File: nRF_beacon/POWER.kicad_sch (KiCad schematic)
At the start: 6 parts, among them U3 NPM1300-QEAA-R7

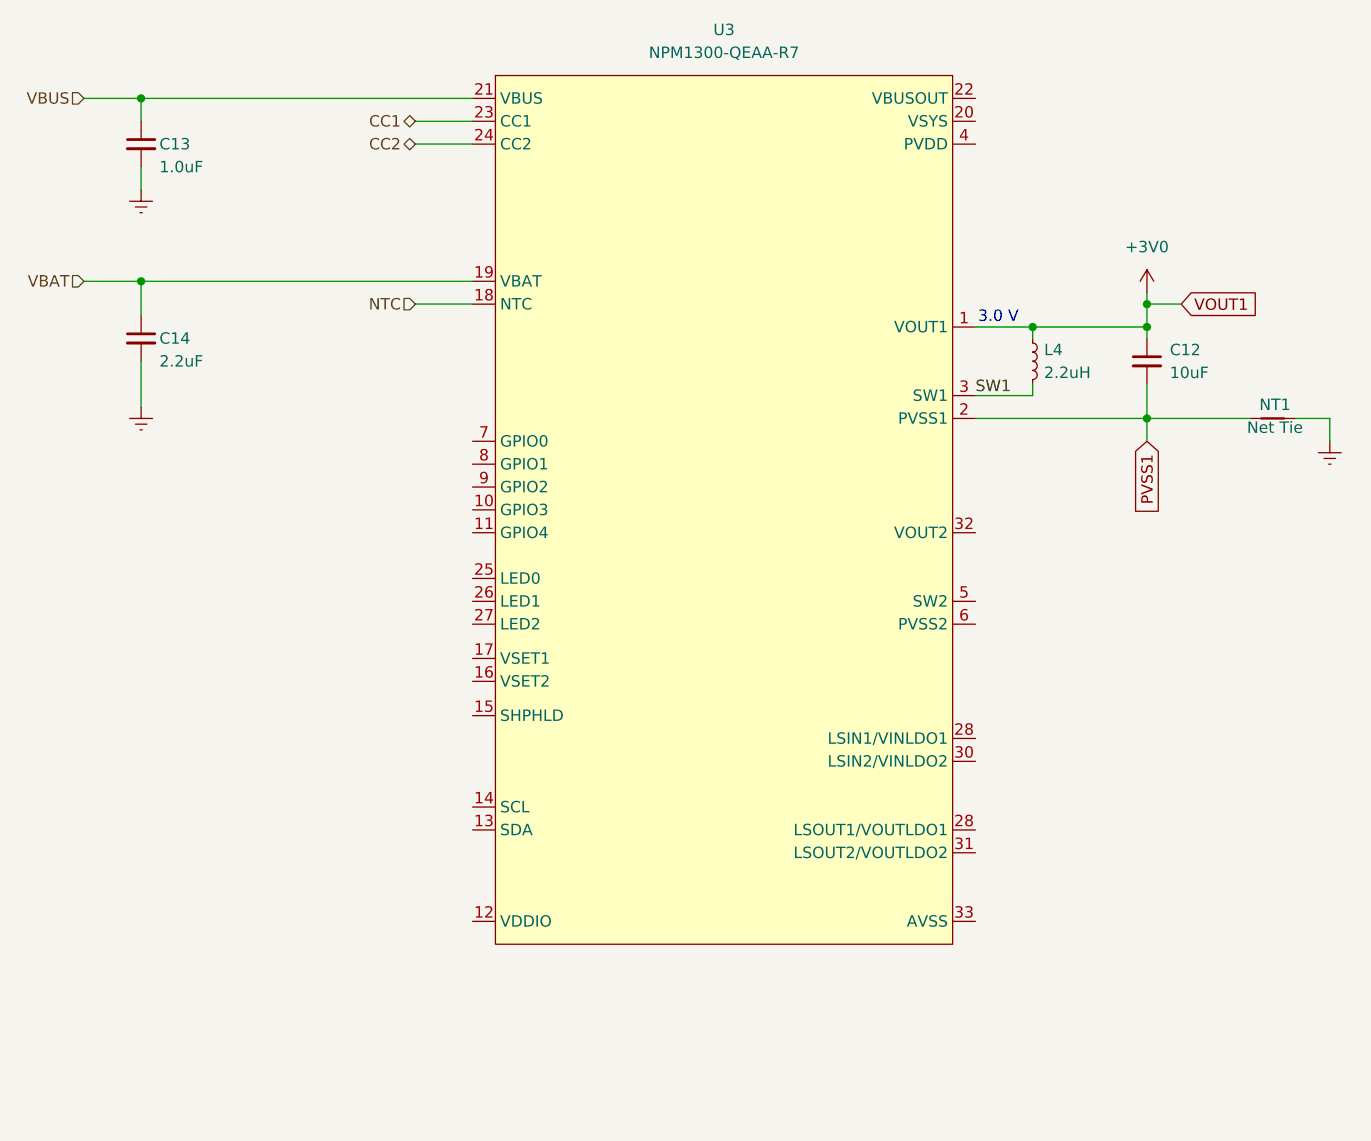
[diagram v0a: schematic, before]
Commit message: Added MPN and footprints for all components on nRF general application
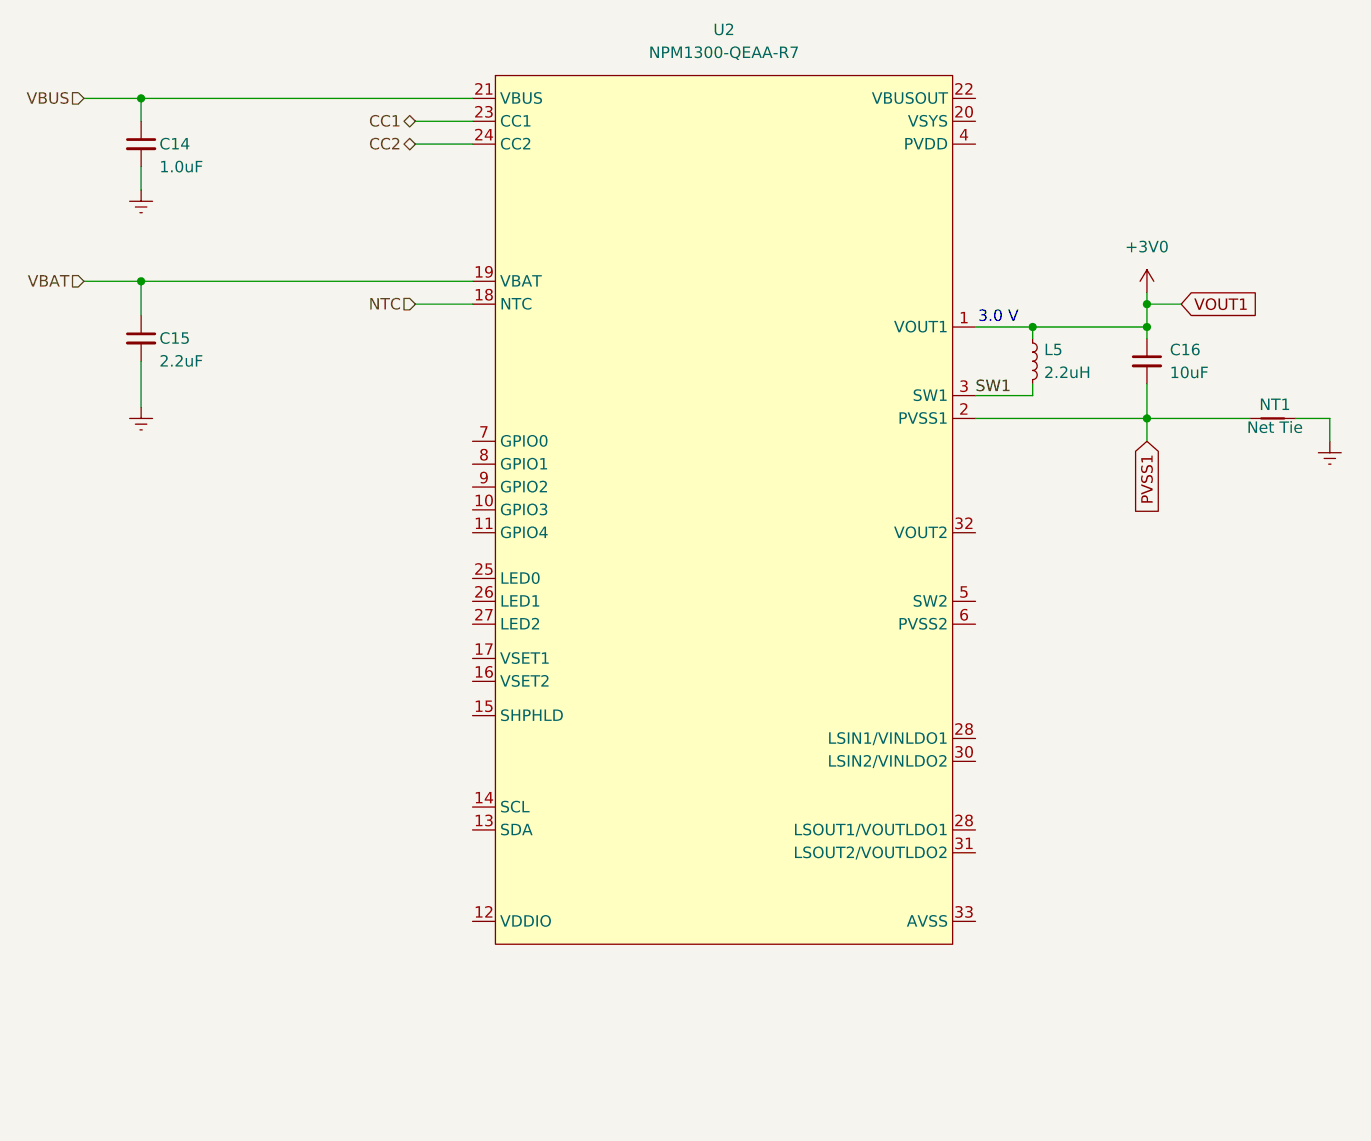
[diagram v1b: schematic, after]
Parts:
- renumbered C13 to C14, C14 to C15, C12 to C16, L4 to L5, U3 to U2
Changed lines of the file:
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@@
 		(dnp no)
 		(fields_autoplaced yes)
-		(property "Reference" "L4"
+		(property "Reference" "L5"
 			(at 184.15 86.3599 0)
 			(effects
@@
 			)
 		)
+		(property "MPN" ""
+			(at 182.88 87.63 0)
+			(effects
+				(font
+					(size 1.27 1.27)
+				)
+				(hide yes)
+			)
+		)
+		(property "Price" ""
+			(at 182.88 87.63 0)
+			(effects
+				(font
+					(size 1.27 1.27)
+				)
+				(hide yes)
+			)
+		)
 		(pin "2"
 		)
@@
 			(project ""
 				(path "/1290e5f5-b91f-4d6e-b440-6b78e8fdc212/1b7d8d32-f2af-4099-9901-f3134d87cd68"
-					(reference "L4")
+					(reference "L5")
 					(unit 1)
 				)
@@
 		(dnp no)
 		(fields_autoplaced yes)
-		(property "Reference" "#PWR016"
+		(property "Reference" "#PWR020"
 			(at 195.58 83.82 0)
 			(effects
@@
 			(project ""
 				(path "/1290e5f5-b91f-4d6e-b440-6b78e8fdc212/1b7d8d32-f2af-4099-9901-f3134d87cd68"
-					(reference "#PWR016")
+					(reference "#PWR020")
 					(unit 1)
 				)
@@
 		(dnp no)
 		(fields_autoplaced yes)
-		(property "Reference" "#PWR021"
+		(property "Reference" "#PWR019"
 			(at 83.82 99.06 0)
 			(effects
@@
 			(project "nRF_beacon"
 				(path "/1290e5f5-b91f-4d6e-b440-6b78e8fdc212/1b7d8d32-f2af-4099-9901-f3134d87cd68"
-					(reference "#PWR021")
+					(reference "#PWR019")
 					(unit 1)
 				)
@@
 		(on_board yes)
 		(dnp no)
-		(property "Reference" "C14"
+		(property "Reference" "C15"
 			(at 85.852 85.09 0)
 			(effects
@@
 			)
 		)
+		(property "MPN" ""
+			(at 83.82 85.09 0)
+			(effects
+				(font
+					(size 1.27 1.27)
+				)
+				(hide yes)
+			)
+		)
+		(property "Price" ""
+			(at 83.82 85.09 0)
+			(effects
+				(font
+					(size 1.27 1.27)
+				)
+				(hide yes)
+			)
+		)
 		(pin "1"
 		)
@@
 			(project "nRF_beacon"
 				(path "/1290e5f5-b91f-4d6e-b440-6b78e8fdc212/1b7d8d32-f2af-4099-9901-f3134d87cd68"
-					(reference "C14")
+					(reference "C15")
 					(unit 1)
 				)
@@
 		(dnp no)
 		(fields_autoplaced yes)
-		(property "Reference" "U3"
+		(property "Reference" "U2"
 			(at 148.59 50.8 0)
 			(effects
@@
 			)
 		)
+		(property "MPN" ""
+			(at 147.32 102.87 0)
+			(effects
+				(font
+					(size 1.27 1.27)
+				)
+				(hide yes)
+			)
+		)
+		(property "Price" ""
+			(at 147.32 102.87 0)
+			(effects
+				(font
+					(size 1.27 1.27)
+				)
+				(hide yes)
+			)
+		)
 		(pin "7"
 		)
@@
 			(project "nRF_beacon"
 				(path "/1290e5f5-b91f-4d6e-b440-6b78e8fdc212/1b7d8d32-f2af-4099-9901-f3134d87cd68"
-					(reference "U3")
+					(reference "U2")
 					(unit 1)
 				)
@@
 		(dnp no)
 		(fields_autoplaced yes)
-		(property "Reference" "#PWR017"
+		(property "Reference" "#PWR021"
 			(at 215.9 102.87 0)
 			(effects
@@
 			(project ""
 				(path "/1290e5f5-b91f-4d6e-b440-6b78e8fdc212/1b7d8d32-f2af-4099-9901-f3134d87cd68"
-					(reference "#PWR017")
+					(reference "#PWR021")
 					(unit 1)
 				)
@@
 		(on_board yes)
 		(dnp no)
-		(property "Reference" "C13"
+		(property "Reference" "C14"
 			(at 85.852 63.5 0)
 			(effects
@@
 			)
 		)
+		(property "MPN" ""
+			(at 83.82 63.5 0)
+			(effects
+				(font
+					(size 1.27 1.27)
+				)
+				(hide yes)
+			)
+		)
+		(property "Price" ""
+			(at 83.82 63.5 0)
+			(effects
+				(font
+					(size 1.27 1.27)
+				)
+				(hide yes)
+			)
+		)
 		(pin "1"
 		)
@@
 			(project ""
 				(path "/1290e5f5-b91f-4d6e-b440-6b78e8fdc212/1b7d8d32-f2af-4099-9901-f3134d87cd68"
-					(reference "C13")
+					(reference "C14")
 					(unit 1)
 				)
@@
 			)
 		)
+		(property "MPN" ""
+			(at 209.55 93.98 0)
+			(effects
+				(font
+					(size 1.27 1.27)
+				)
+				(hide yes)
+			)
+		)
+		(property "Price" ""
+			(at 209.55 93.98 0)
+			(effects
+				(font
+					(size 1.27 1.27)
+				)
+				(hide yes)
+			)
+		)
 		(pin "1"
 		)
@@
 		(dnp no)
 		(fields_autoplaced yes)
-		(property "Reference" "C12"
+		(property "Reference" "C16"
 			(at 198.12 86.3662 0)
 			(effects
@@
 			)
 		)
+		(property "MPN" ""
+			(at 195.58 87.63 0)
+			(effects
+				(font
+					(size 1.27 1.27)
+				)
+				(hide yes)
+			)
+		)
+		(property "Price" ""
+			(at 195.58 87.63 0)
+			(effects
+				(font
+					(size 1.27 1.27)
+				)
+				(hide yes)
+			)
+		)
 		(pin "2"
 		)
@@
 			(project ""
 				(path "/1290e5f5-b91f-4d6e-b440-6b78e8fdc212/1b7d8d32-f2af-4099-9901-f3134d87cd68"
-					(reference "C12")
+					(reference "C16")
 					(unit 1)
 				)
@@
 		(dnp no)
 		(fields_autoplaced yes)
-		(property "Reference" "#PWR020"
+		(property "Reference" "#PWR018"
 			(at 83.82 74.93 0)
 			(effects
@@
 			(project ""
 				(path "/1290e5f5-b91f-4d6e-b440-6b78e8fdc212/1b7d8d32-f2af-4099-9901-f3134d87cd68"
-					(reference "#PWR020")
-					(unit 1)
-				)
+					(reference "#PWR018")
+					(unit 1)
+				)

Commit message: Added buck configuration for AUDIO 3.3V power. Removed USB input
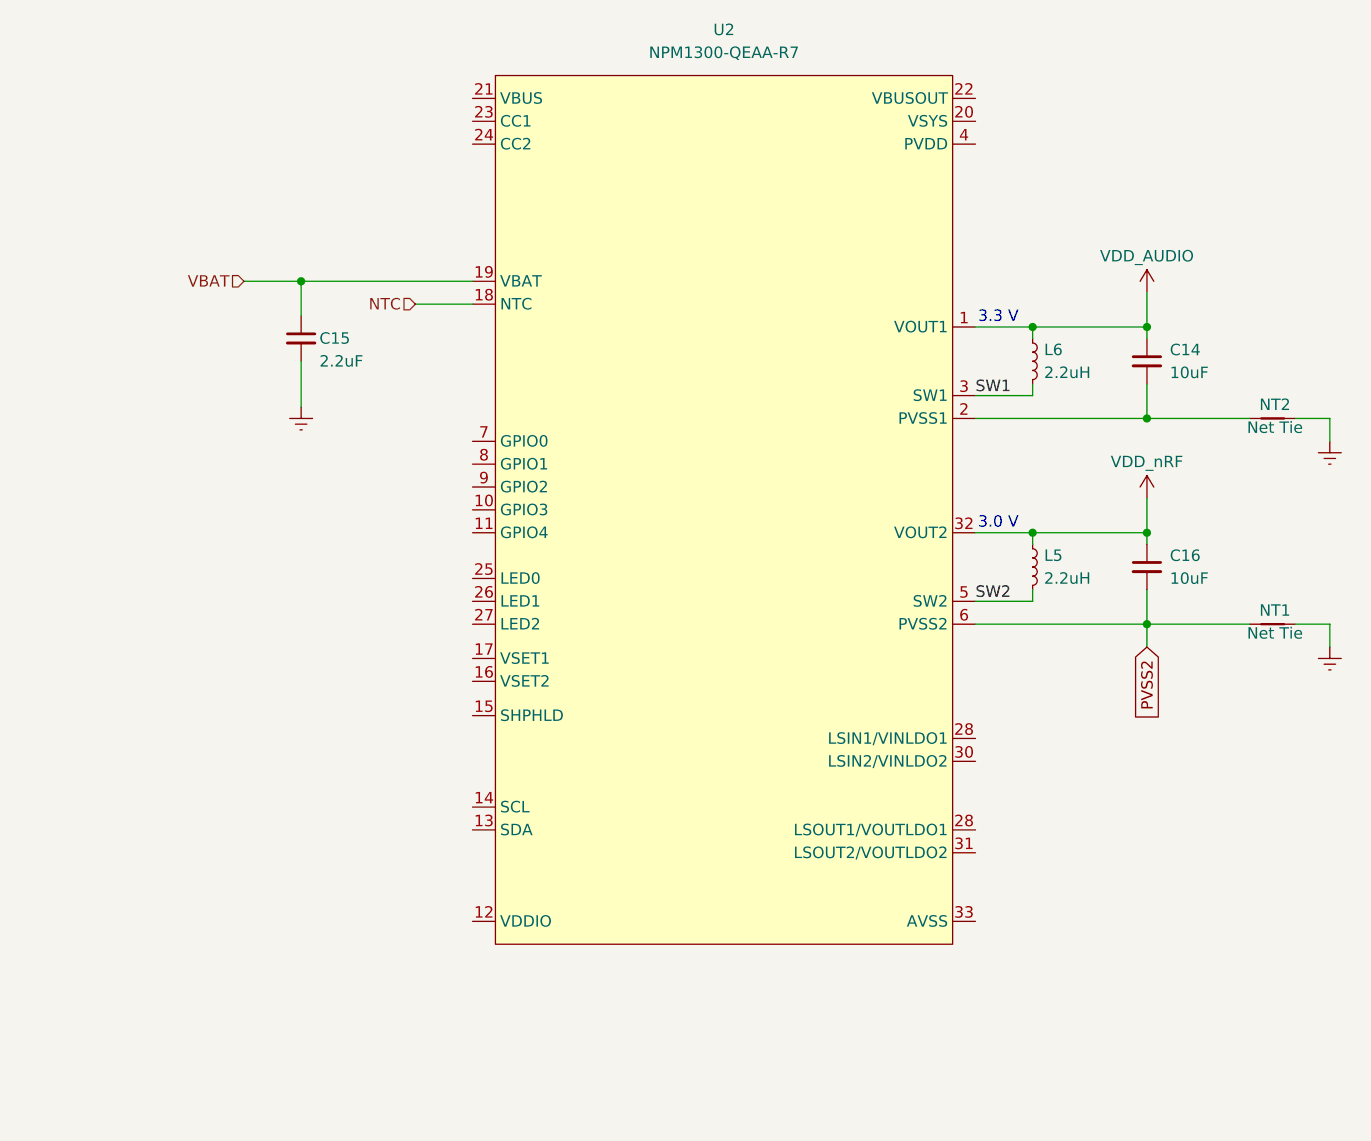
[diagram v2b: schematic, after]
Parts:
- added L6: 2.2uH, symbol Device:L_Small
- added NT2: Net Tie, symbol Device:NetTie_2
- C14: value 1.0uF -> 10uF
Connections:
- net Earth: now also NT2.2; no longer C14.2
- net SW1: now also L6.2; no longer L5.2
- net VDD_nRF: now reaches U2.32 (VOUT2)
- net VDD_nRF: now also C16.1, L5.1
- net SW2: now reaches U2.5 (SW2)
- net SW2: now also L5.2
- net PVSS2: now reaches U2.6 (PVSS2)
- net PVSS2: now also C16.2, NT1.1
- removed net +3V0: C16.1, L5.1, U2.1 (VOUT1)
- net CC1: no longer names the net of U2.23 (CC1)
- net CC2: no longer names the net of U2.24 (CC2)
- removed net PVSS1: C16.2, NT1.1, U2.2 (PVSS1)
- net VBUS: no longer names the net of U2.21 (VBUS)
- net VBUS: no longer C14.1
- new net: C14.2, NT2.1, U2.2 (PVSS1)
- new net VDD_AUDIO: C14.1, L6.1, U2.1 (VOUT1)
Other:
- note added: "3.3 V"
- moved on the sheet: C15, C16, L5, NT1

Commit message: Updated nPM schematic. Added TWI and debug connector
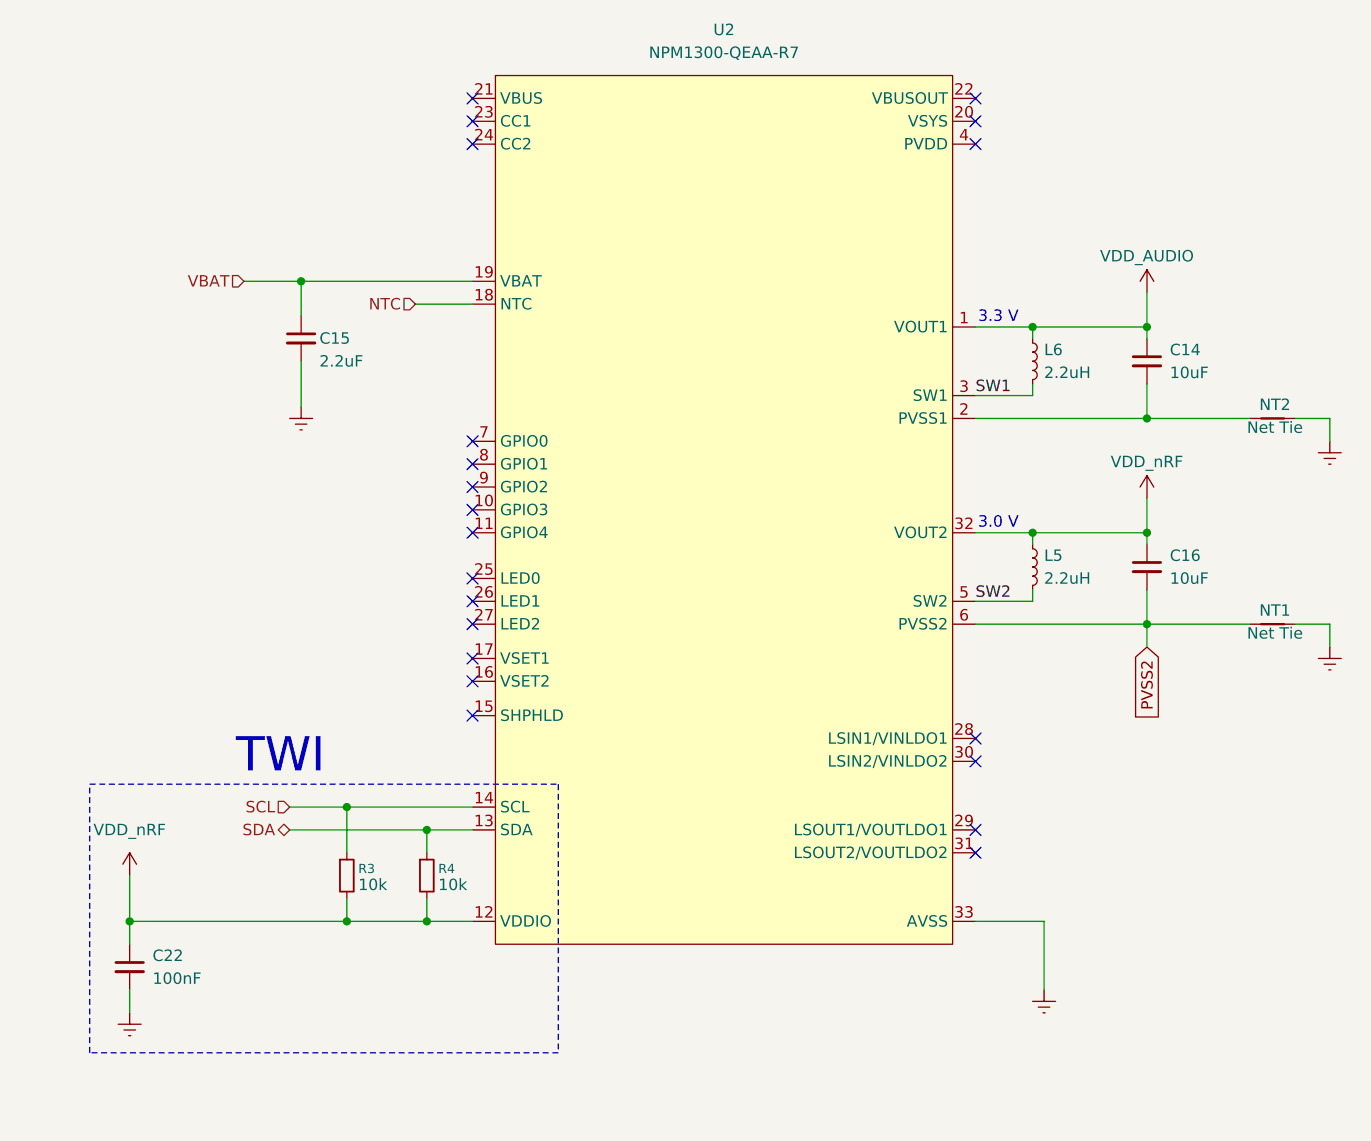
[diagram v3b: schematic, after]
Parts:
- added C22: 100nF, symbol Device:C_Small
- added R3, R4: 10k, symbol Device:R_Small
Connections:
- net Earth: now also U2.33 (AVSS), C22.2
- net VDD_nRF: now also U2.12 (VDDIO), C22.1, R3.2, R4.2
- net SDA: now reaches U2.13 (SDA)
- net SDA: now also R4.1
- net SCL: now reaches U2.14 (SCL)
- net SCL: now also R3.1
- no-connect marks 0 -> 21
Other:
- note added: "TWI"

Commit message: Added LEDs and BUCK supply from VSYS
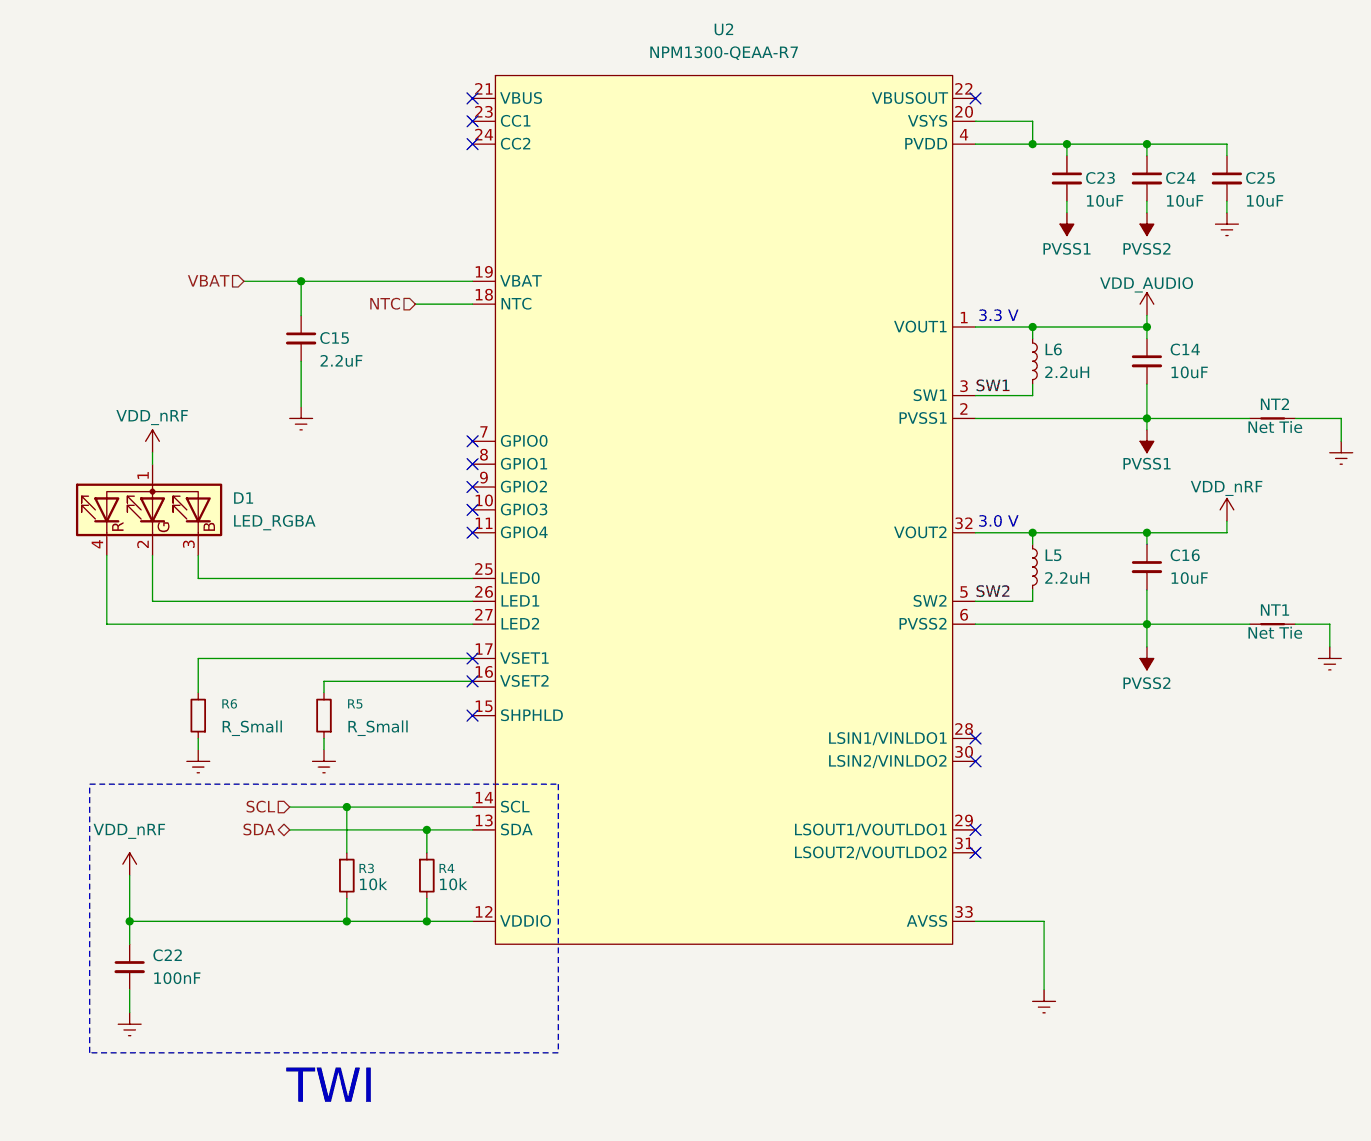
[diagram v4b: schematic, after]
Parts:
- added C23, C24, C25: 10uF, symbol Device:C_Small
- added D1: LED_RGBA, symbol Device:LED_RGBA
- added R5, R6: R_Small, symbol Device:R_Small
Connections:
- net Earth: now also C25.2, R5.1, R6.1
- net PVSS2: now also C24.2
- net VDD_nRF: now also D1.1 (A)
- net PVSS1: now reaches C14.2, NT2.1, U2.2 (PVSS1)
- net PVSS1: now also C23.2
- net at U2.16 (VSET2): now also R5.2
- net at U2.17 (VSET1): now also R6.2
- net at U2.20 (VSYS): now also U2.4 (PVDD), C23.1, C24.1, C25.1
- net at U2.25 (LED0): now also D1.3 (BK)
- net at U2.26 (LED1): now also D1.2 (GK)
- net at U2.27 (LED2): now also D1.4 (RK)
- no-connect marks 21 -> 16
